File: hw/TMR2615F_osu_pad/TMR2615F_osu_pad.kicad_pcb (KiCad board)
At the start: 4 copper layers, 70.1 x 60 mm, 164 parts, among them J1 TYPE-C-31-M-12, J2 TYPE-C-31-M-12, J3 TYPE-C-31-M-12, J4 XY-SH1_0-4A61, J5 Conn_01x10, J6 Conn_01x23, J7 Conn_01x06, J8 Conn_01x04, SW1 SKSGPAE010, SW2 SKSGPAE010, SW3 CPG151101S11-16, SW4 CPG151101S11-16, SW5 CPG151101S11-16, SW6 CPG151101S11-16, SW7 CPG151101S11-16, SW8 CPG151101S11-16, U1 SRV05-4A, U10 AT32F405RBT7-7, U11 TMUX1574RSVR, U12 SK6812MINI-E, U13 TMR2615x, U14 SK6812MINI-E, U15 TMR2615x, U16 SK6812MINI-E, U17 TMR2615x, U18 SK6812MINI-E, U19 TMR2615x, U2 LM66100DCK, U20 SK6812MINI-E, U21 TMR2615x, U22 SK6812MINI-E, U23 TMR2615x, U24 SK6812MINI-E, U3 AP22653W6-7, U4 TPS7A4700, U5 SRV05-4A, U6 SRV05-4A, U7 LM66100DCK, U8 XC6206P332MR, U9 SRV05-4A, X1 X322512MSB4SI

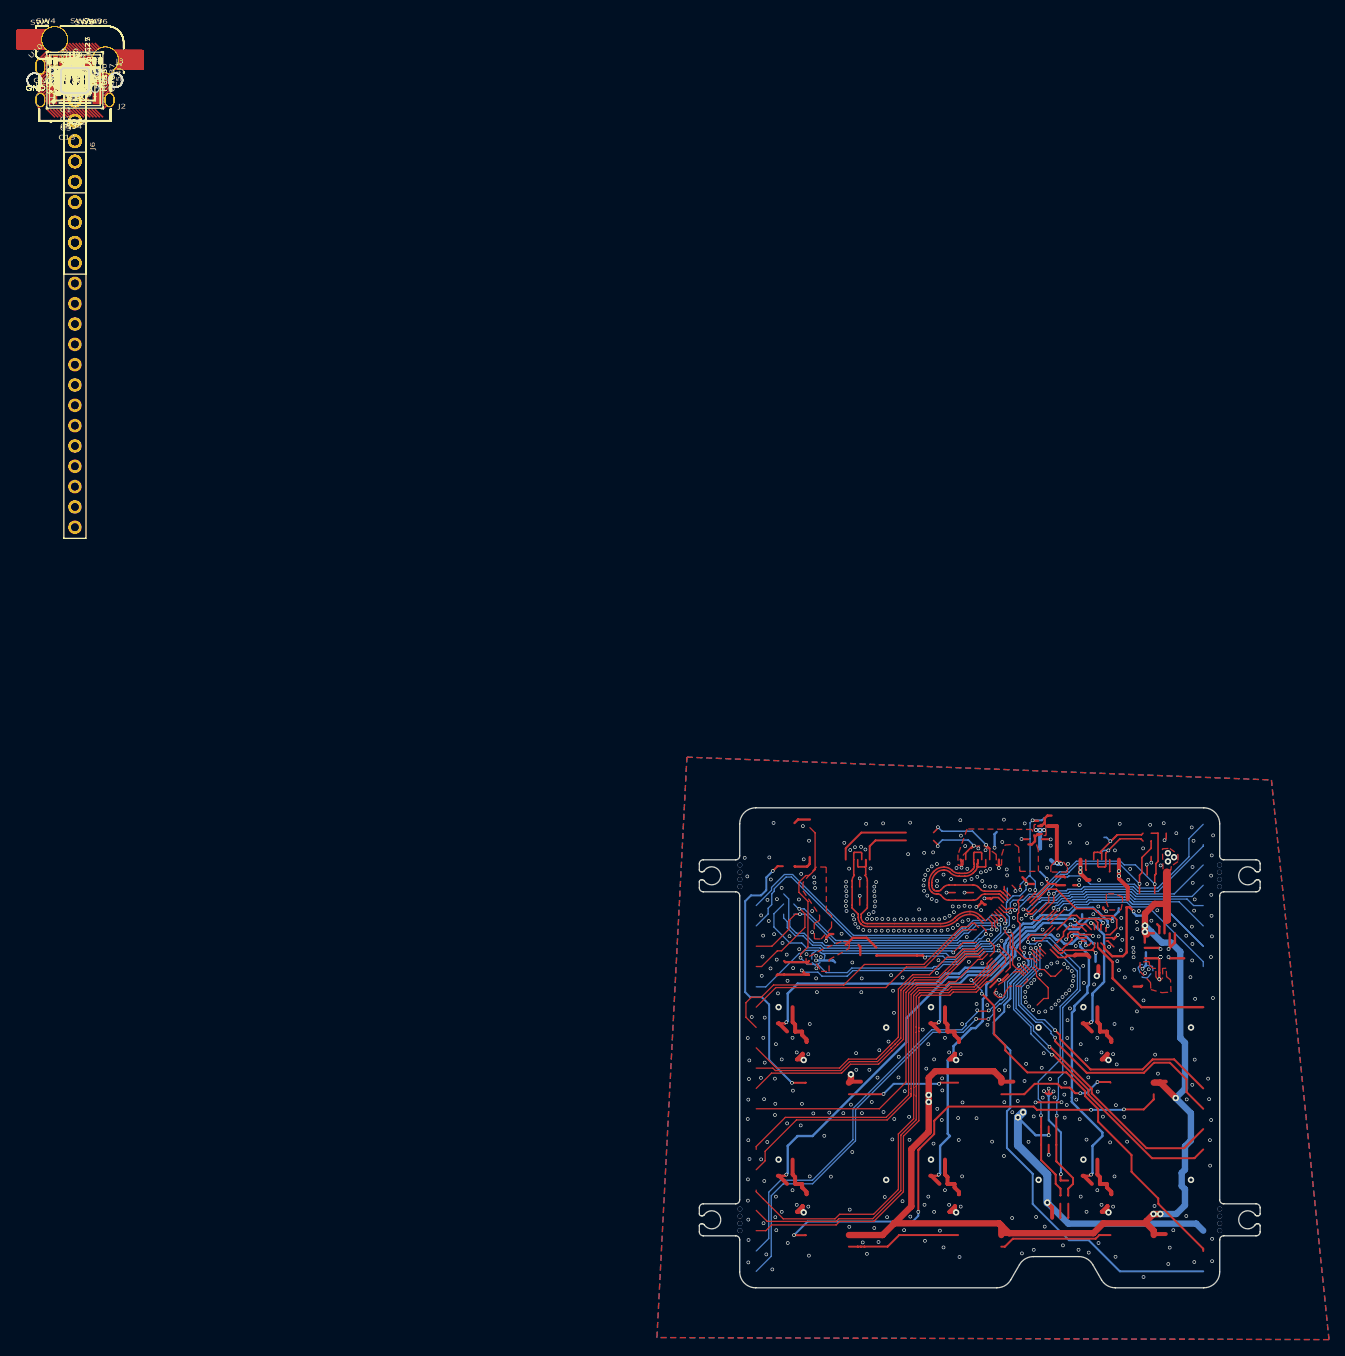
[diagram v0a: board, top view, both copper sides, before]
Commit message: Update TMR2615F_osu_pad layout, project settings, and STEP export
Board layout revision plus refreshed STEP. Project file adds MPN and
Manufacturer BOM fields, repoints bom_export_filename off an absolute
D:\ path to output/TMR2615F_osu_pad.csv, and sets the STEP output name.

Co-Authored-By: Claude Opus 5 (1M context) <noreply@anthropic.com>
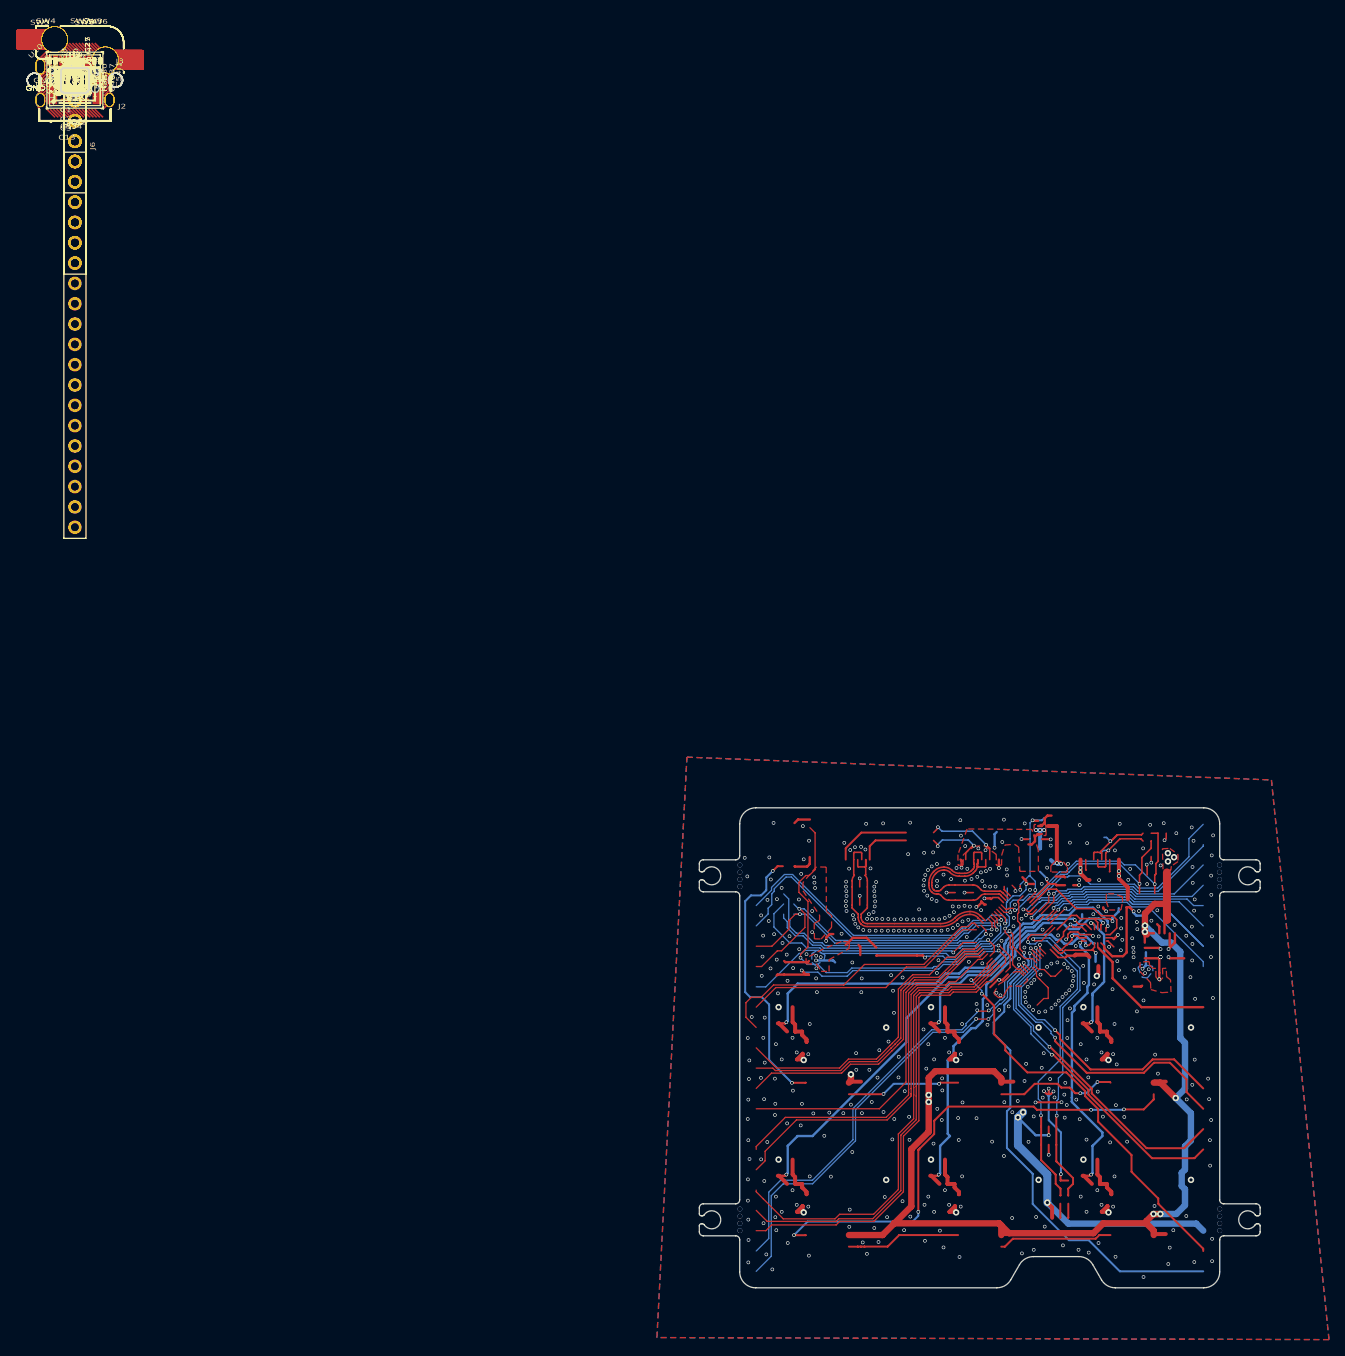
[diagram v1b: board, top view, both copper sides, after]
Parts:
- added G*** (x3): LOGO, LOGO, B.Cu at (0.00, 0.00)
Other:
- board text added: "TMR Macropad TMR2615F + AT32F405"
